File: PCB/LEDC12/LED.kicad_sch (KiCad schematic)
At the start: 38 parts, among them J1 Reset, J2 Wago, J3 USB-C-Socket-H, J4 TC2030-USB-NL-DS, SW1 Button, U1 ESP32-S3-MINI-1, U2 IRMHF384, U3 ICS43434_MEMS_Mic, U4 TPS562243

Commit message: Margins tidy
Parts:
- R8: value 100k -> 150k 1%; MPN C106224 -> C310173
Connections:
- net DC: now also R8.2; no longer R8.1
- net EN: now also R8.1; no longer R8.2
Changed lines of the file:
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@@
+	)
+	(symbol
+		(lib_id "Device:R")
+		(at 207.01 152.4 270)
+		(unit 1)
+		(exclude_from_sim no)
+		(in_bom yes)
+		(on_board yes)
+		(dnp no)
+		(property "Reference" "R8"
+			(at 205.74 152.4 90)
+			(effects
+				(font
+					(size 1.27 1.27)
+				)
+				(justify left)
+			)
+		)
+		(property "Value" "150k 1%"
+			(at 205.486 154.686 90)
+			(effects
+				(font
+					(size 1.27 1.27)
+				)
+				(justify left)
+			)
+		)
+		(property "Footprint" "RevK:R_0201"
+			(at 207.01 150.622 90)
+			(effects
+				(font
+					(size 1.27 1.27)
+				)
+				(hide yes)
+			)
+		)
+		(property "Datasheet" "~"
+			(at 207.01 152.4 0)
+			(effects
+				(font
+					(size 1.27 1.27)
+				)
+				(hide yes)
+			)
+		)
+		(property "Description" "Resistor"
+			(at 207.01 152.4 0)
+			(effects
+				(font
+					(size 1.27 1.27)
+				)
+				(hide yes)
+			)
+		)
+		(property "MPN" "C310173"
+			(at 207.01 152.4 0)
+			(effects
+				(font
+					(size 1.27 1.27)
+				)
+				(hide yes)
+			)
+		)
+		(pin "1"
+		)
+		(pin "2"
+		)
+		(instances
+			(project "LED"
+				(path "/46c350bb-7de4-4e81-aafd-4af55e37aab0"
+					(reference "R8")
+					(unit 1)
+				)
+			)
+		)
 	)
 	(symbol
@@
 					(unit 1)
 				)
-			)
-		)
-	)
-	(symbol
-		(lib_id "Device:R")
-		(at 207.01 152.4 90)
-		(unit 1)
-		(exclude_from_sim no)
-		(in_bom yes)
-		(on_board yes)
-		(dnp no)
-		(property "Reference" "R8"
-			(at 207.137 150.114 90)
-			(effects
-				(font
-					(size 1.27 1.27)
-				)
-			)
-		)
-		(property "Value" "100k"
-			(at 207.137 152.4 90)
-			(effects
-				(font
-					(size 1.27 1.27)
-				)
-			)
-		)
-		(property "Footprint" "RevK:R_0201"
-			(at 207.01 154.178 90)
-			(effects
-				(font
-					(size 1.27 1.27)
-				)
-				(hide yes)
-			)
-		)
-		(property "Datasheet" "~"
-			(at 207.01 152.4 0)
-			(effects
-				(font
-					(size 1.27 1.27)
-				)
-				(hide yes)
-			)
-		)
-		(property "Description" "Resistor"
-			(at 207.01 152.4 0)
-			(effects
-				(font
-					(size 1.27 1.27)
-				)
-				(hide yes)
-			)
-		)
-		(property "MPN" "C106224"
-			(at 207.01 152.4 90)
-			(effects
-				(font
-					(size 1.27 1.27)
-				)
-				(hide yes)
-			)
-		)
-		(pin "1"
-		)
-		(pin "2"
-		)
-		(instances
-			(project "LED"
-				(path "/46c350bb-7de4-4e81-aafd-4af55e37aab0"
-					(reference "R8")
-					(unit 1)
-				)

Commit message: Remaker
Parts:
- added FID1: Fiducial, Fiducial:Fiducial_1mm_Mask2mm, symbol Mechanical:Fiducial
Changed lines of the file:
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@@
 		)
 		(property "Value" "150k 1%"
-			(at 205.486 154.686 90)
+			(at 203.962 150.114 90)
 			(effects
 				(font
@@
 					(unit 1)
 				)
+			)
+		)
+	)
+	(symbol
+		(lib_id "Mechanical:Fiducial")
+		(at 32.385 160.02 0)
+		(unit 1)
+		(exclude_from_sim no)
+		(in_bom no)
+		(on_board yes)
+		(dnp no)
+		(fields_autoplaced yes)
+		(property "Reference" "FID1"
+			(at 34.544 158.8078 0)
+			(effects
+				(font
+					(size 1.27 1.27)
+				)
+				(justify left)
+			)
+		)
+		(property "Value" "Fiducial"
+			(at 34.544 161.2321 0)
+			(effects
+				(font
+					(size 1.27 1.27)
+				)
+				(justify left)
+			)
+		)
+		(property "Footprint" "Fiducial:Fiducial_1mm_Mask2mm"
+			(at 32.385 160.02 0)
+			(effects
+				(font
+					(size 1.27 1.27)
+				)
+				(hide yes)
+			)
+		)
+		(property "Datasheet" "~"
+			(at 32.385 160.02 0)
+			(effects
+				(font
+					(size 1.27 1.27)
+				)
+				(hide yes)
+			)
+		)
+		(property "Description" "Fiducial Marker"
+			(at 32.385 160.02 0)
+			(effects
+				(font
+					(size 1.27 1.27)
+				)
+				(hide yes)
+			)
+		)
+		(instances
+			(project ""
+				(path "/46c350bb-7de4-4e81-aafd-4af55e37aab0"
+					(reference "FID1")
+					(unit 1)
+				)

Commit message: As ordered today
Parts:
- added C2, C3, C4: 100nF, RevK:C_0201, symbol Device:C
- C1: footprint RevK:C_0402 -> RevK:C_0201
- R1, R4: MPN (none) -> C473048
- R2: MPN (none) -> C270346
- R3: MPN (none) -> C423759
- R5: MPN (none) -> C273279
- R6, R7: MPN (none) -> C274341
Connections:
- net +3V3: now also C2.1, C3.1, C4.1
- net GND: now also C2.2, C3.2, C4.2

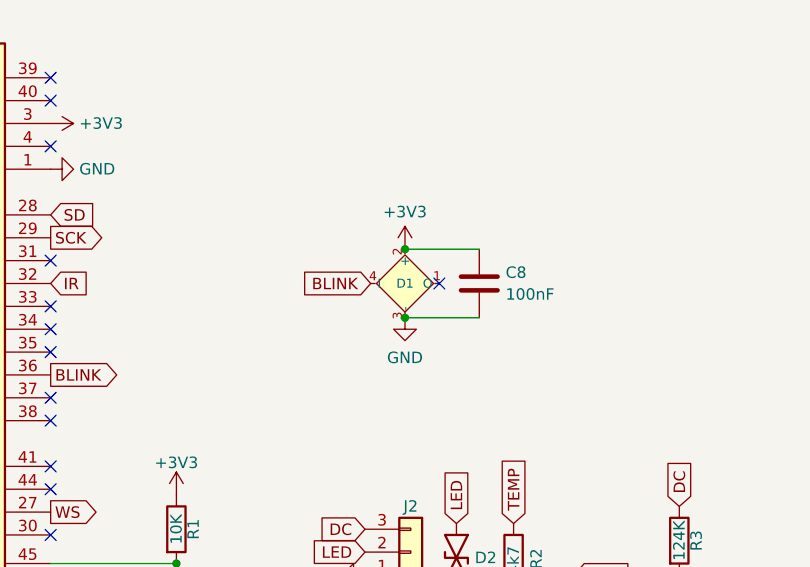
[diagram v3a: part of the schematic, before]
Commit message: New LEDs
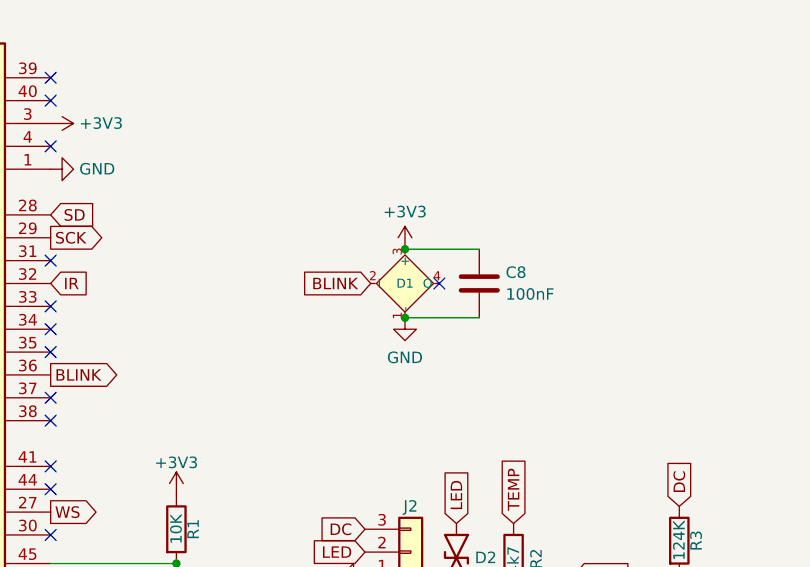
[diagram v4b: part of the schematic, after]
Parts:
- D1: footprint RevK:SMD1010 -> RevK:SMD1615; symbol RevK:WS2812B-1mm -> RevK:WS2812B-1.5mm; MPN C5349953 -> C5349954
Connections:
- net +3V3: now also D1.3 (+); no longer D1.2 (+)
- net BLINK: now also D1.2 (I); no longer D1.4 (I)
- net GND: now also D1.1 (-); no longer D1.3 (-)
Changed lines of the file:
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@@
 	)
 	(symbol
-		(lib_id "RevK:WS2812B-1mm")
+		(lib_id "RevK:WS2812B-1.5mm")
 		(at 105.41 73.66 0)
-		(mirror x)
 		(unit 1)
 		(exclude_from_sim no)
@@
 		)
 		(property "Value" "XL-1010RGBC-WS2812B"
-			(at 106.68 67.945 0)
+			(at 106.68 79.375 0)
 			(effects
 				(font
@@
 			)
 		)
-		(property "Footprint" "RevK:SMD1010"
+		(property "Footprint" "RevK:SMD1615"
 			(at 106.68 66.04 0)
 			(effects
@@
 			)
 		)
-		(property "Datasheet" "https://datasheet.lcsc.com/lcsc/2301111010_XINGLIGHT-XL-1010RGBC-WS2812B_C5349953.pdf"
+		(property "Datasheet" "https://www.lcsc.com/datasheet/C5349954.pdf"
 			(at 106.68 64.135 0)
 			(effects
@@
 			)
 		)
-		(property "MPN" "C5349953"
+		(property "MPN" "C5349954"
 			(at 106.68 62.23 0)
 			(effects
